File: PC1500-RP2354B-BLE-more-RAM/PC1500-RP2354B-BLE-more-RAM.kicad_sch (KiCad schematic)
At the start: 41 parts, among them J1 microSD, J2 USB-C (programming/debug), J3 PC-1500 40-pin cartridge slot, J5 PC1500_SENSE_JUMPER, J7 SWD_I2C_HEADER, SW1 BOOTSEL, U1 RP2354B, U10 TCA9406DCUR, U2 AS6C1008-55TINL, U3 SLG46826V, U4 AP2112K-3.3, U5 MCP6541T-I/LT, U8 BGM220SC22WGA2, U9 SLG46826V, X1 12MHz (Abracon ABM8-272-T3)

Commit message: More-RAM card: BLE_MODULE_WAKE (GPIO27 to BGM220S PB03); I2C pull-ups
- BLE_MODULE_WAKE: the MCU-to-module wake (an EM4 wake pin on the
  module), lost in the bus rewire. Pads updated; routing left for later.
- R25/R26: 1.5K pull-ups from SDA/SCL to +3V3.

Co-Authored-By: Claude Opus 5.5 <noreply@anthropic.com>
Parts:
- added R25, R26: 1.5K, Resistor_SMD:R_0201_0603Metric, symbol Device:R
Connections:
- net +3V3: now also R25.1, R26.1
- net SCL: now also R26.2
- net SCL_GP: no longer J7.1 (Pin_1)
- net SDA: now also R25.2
- net SDA_GP: no longer J7.3 (Pin_3)
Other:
- moved on the sheet: J7

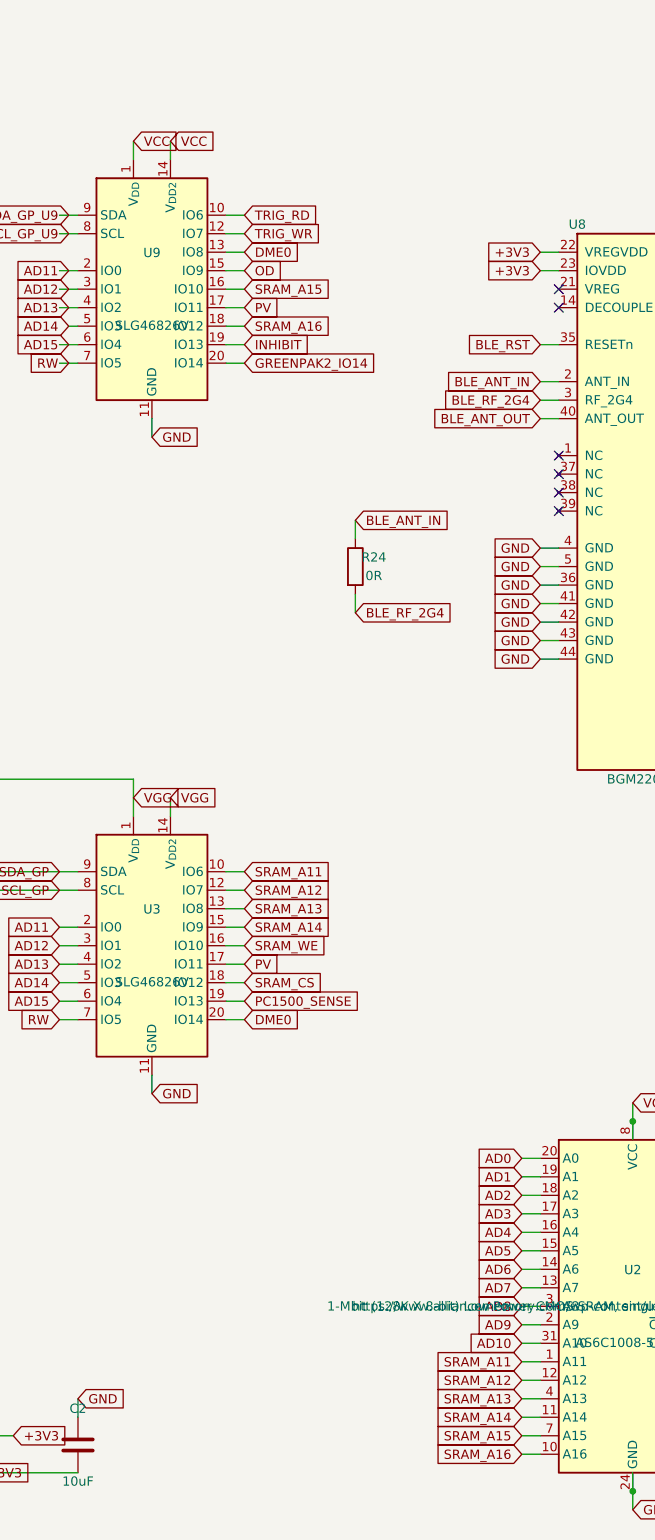
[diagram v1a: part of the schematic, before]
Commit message: More-RAM card schematic: SRAM A11-A13 from the bus, GP1 drives A14-A16, INHIBIT on GP1, GP2 on VGG
- SRAM A11-A13 come straight from AD11-AD13; GP1 (U3) IO7/IO8/IO9 drive
  SRAM_A14/15/16 (the card GP1 design).
- INHIBIT (J3 pin 15) moved to GP1 IO6 (U3 pin 10); GP2 IO10/IO12/IO13 are
  no-connects.
- GP2 (U9) VDD/VDD2 moved from VCC to VGG, as on the dongle: both GreenPAKs
  keep their state through power-off.
Schematic only; the PCB still has the old nets and needs re-routing.

Co-Authored-By: Claude Opus 5.5 <noreply@anthropic.com>
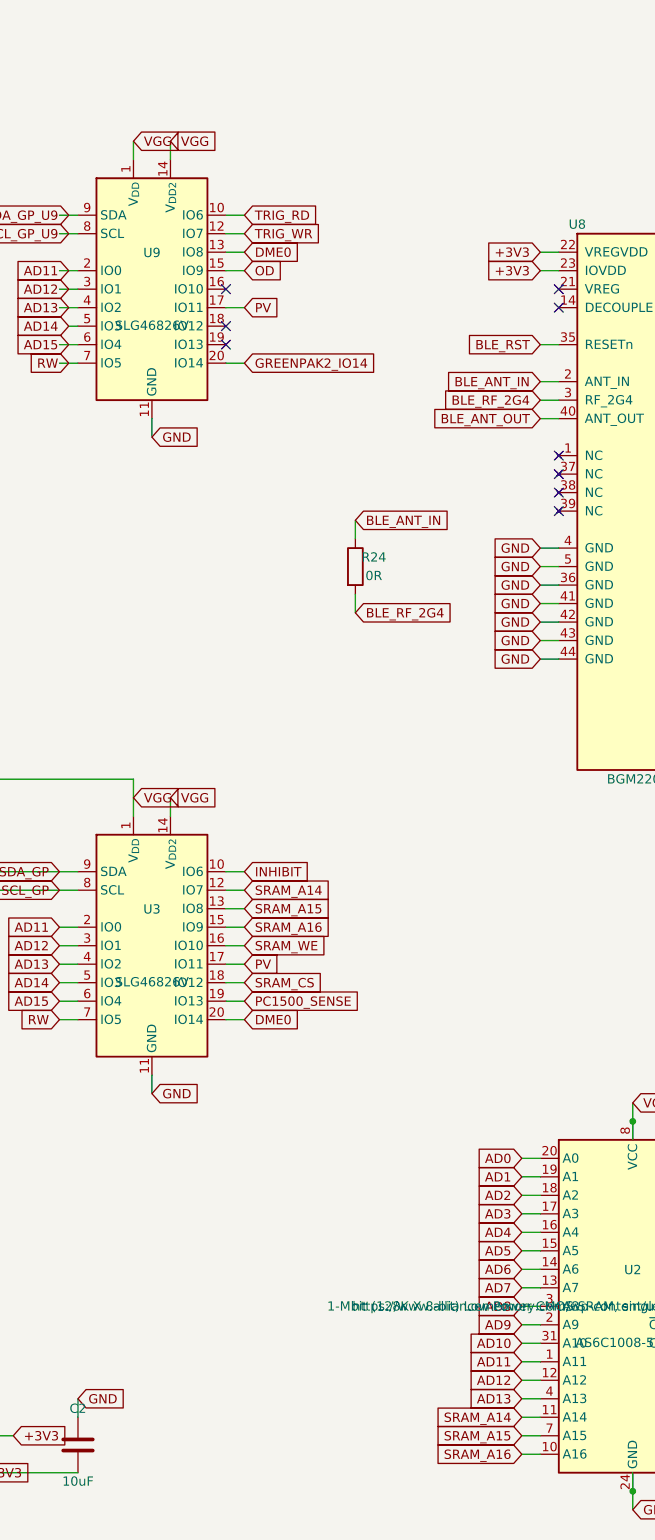
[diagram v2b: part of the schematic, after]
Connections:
- net AD11: now also U2.1 (A11)
- net AD12: now also U2.12 (A12)
- net AD13: now also U2.4 (A13)
- net INHIBIT: now also U3.10 (IO6); no longer U9.19 (IO13)
- net SRAM_A14: now also U3.12 (IO7); no longer U3.15 (IO9)
- net SRAM_A15: now also U3.13 (IO8); no longer U9.16 (IO10)
- net SRAM_A16: now also U3.15 (IO9); no longer U9.18 (IO12)
- net VCC: no longer U9.1 (V_{DD}), U9.14 (V_{DD2})
- net VGG: now also U9.1 (V_{DD}), U9.14 (V_{DD2})
- removed net SRAM_A11: U2.1 (A11), U3.10 (IO6)
- removed net SRAM_A12: U2.12 (A12), U3.12 (IO7)
- removed net SRAM_A13: U2.4 (A13), U3.13 (IO8)
- no-connect marks 29 -> 32
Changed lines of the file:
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@@
 		)
 	)
-	(wire
-		(pts
-			(xy 139.7 95.25) (xy 142.24 95.25)
-		)
-		(stroke
-			(width 0)
-			(type default)
-		)
+	(no_connect
+		(at 139.7 95.25)
 	)
 	(wire
@@
 		)
 	)
-	(wire
-		(pts
-			(xy 139.7 90.17) (xy 142.24 90.17)
-		)
-		(stroke
-			(width 0)
-			(type default)
-		)
+	(no_connect
+		(at 139.7 90.17)
 	)
 	(wire
@@
 		)
 	)
-	(wire
-		(pts
-			(xy 139.7 97.79) (xy 142.24 97.79)
-		)
-		(stroke
-			(width 0)
-			(type default)
-		)
+	(no_connect
+		(at 139.7 97.79)
 	)
 	(wire
@@
 		)
 	)
+	(global_label "INHIBIT"
+		(shape input)
+		(at 142.24 170.18 0)
+		(effects
+			(font
+				(size 1.27 1.27)
+			)
+			(justify left)
+		)
+		(property "Intersheetrefs" "${INTERSHEET_REFS}"
+			(at 142.24 170.18 0)
+			(hide yes)
+			(show_name no)
+			(do_not_autoplace no)
+			(effects
+				(font
+					(size 1.27 1.27)
+				)
+			)
+		)
+	)
 	(wire
 		(pts
@@
 		)
 	)
-	(global_label "VCC"
+	(global_label "VGG"
 		(shape input)
 		(at 132.08 69.85 0)
@@
 		)
 	)
-	(global_label "SRAM_A12"
+	(global_label "AD12"
 		(shape input)
 		(at 180.34 240.03 180)
@@
 		)
 	)
-	(global_label "SRAM_A15"
-		(shape input)
-		(at 142.24 90.17 0)
-		(effects
-			(font
-				(size 1.27 1.27)
-			)
-			(justify left)
-		)
-		(property "Intersheetrefs" "${INTERSHEET_REFS}"
-			(at 142.24 90.17 0)
-			(hide yes)
-			(show_name no)
-			(do_not_autoplace no)
-			(effects
-				(font
-					(size 1.27 1.27)
-				)
-			)
-		)
-	)
 	(global_label "AD8"
 		(shape input)
@@
 		)
 	)
-	(global_label "SRAM_A13"
+	(global_label "AD13"
 		(shape input)
 		(at 180.34 242.57 180)
@@
 		)
 	)
-	(global_label "SRAM_A12"
+	(global_label "SRAM_A14"
 		(shape input)
 		(at 142.24 172.72 0)
@@
 		)
 	)
-	(global_label "INHIBIT"
-		(shape input)
-		(at 142.24 97.79 0)
-		(effects
-			(font
-				(size 1.27 1.27)
-			)
-			(justify left)
-		)
-		(property "Intersheetrefs" "${INTERSHEET_REFS}"
-			(at 142.24 97.79 0)
-			(hide yes)
-			(show_name no)
-			(do_not_autoplace no)
-			(effects
-				(font
-					(size 1.27 1.27)
-				)
-			)
-		)
-	)
 	(global_label "TRIG_WR"
 		(shape input)
@@
 		)
 	)
-	(global_label "SRAM_A14"
+	(global_label "SRAM_A16"
 		(shape input)
 		(at 142.24 177.8 0)
@@
 		)
 	)
-	(global_label "SRAM_A11"
-		(shape input)
-		(at 142.24 170.18 0)
-		(effects
-			(font
-				(size 1.27 1.27)
-			)
-			(justify left)
-		)
-		(property "Intersheetrefs" "${INTERSHEET_REFS}"
-			(at 142.24 170.18 0)
-			(hide yes)
-			(show_name no)
-			(do_not_autoplace no)
-			(effects
-				(font
-					(size 1.27 1.27)
-				)
-			)
-		)
-	)
 	(global_label "SD_CS"
 		(shape input)
@@
 		)
 	)
-	(global_label "SRAM_A13"
+	(global_label "SRAM_A15"
 		(shape input)
 		(at 142.24 175.26 0)
@@
 		)
 	)
-	(global_label "SRAM_A11"
+	(global_label "AD11"
 		(shape input)
 		(at 180.34 237.49 180)
@@
 		)
 	)
-	(global_label "VCC"
+	(global_label "VGG"
 		(shape input)
 		(at 127 69.85 0)
@@
 			(hide yes)
 			(show_name no)
-			(do_not_autoplace no)
-			(effects
-				(font
-					(size 1.27 1.27)
-				)
-			)
-		)
-	)
-	(global_label "SRAM_A16"
-		(shape input)
-		(at 142.24 95.25 0)
-		(effects
-			(font
-				(size 1.27 1.27)
-			)
-			(justify left)
-		)
-		(property "Intersheetrefs" "${INTERSHEET_REFS}"
-			(at 142.24 95.25 0)
-			(hide yes)
-			(show_name no)

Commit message: More-RAM card: GP2 INHIBIT/MCU_READY/TRIG_WR_SYS, test points, USB 27R, decoupling, Abracon L2; placed and routed
Schematic:
- INHIBIT from GP2 (U9) IO10; U9 IO14 = MCU_READY -> GPIO25; U9 IO12 =
  TRIG_WR_SYS (7000-7FFF write trigger) -> GPIO24.
- Test points: TP4 on GPIO46; TP9 GP1_IO6, TP10 GP2_IO13, TP11 card-edge PU.
- USB-C D+/D- pairing fixed; R27/R28 27R series resistors.
- Decoupling per Raspberry Pi's "Hardware design with RP2350": 100nF per
  RP2354B power pin, 4.7uF on VREG_VIN and DVDD, R29 33R + C27 4.7uF on
  VREG_AVDD (FLG5). One 100nF per GreenPAK at VDD, two on the SRAM.
- L2 = Abracon AOTA-B201610S3R3-101-T (LCSC C42411119) on a new
  Sharp-PC-Footprints:L_Abracon_AOTA-B201610 footprint, generated by
  tools/gen_fp_abracon_aota_b201610.py from Abracon's land pattern.
- TP values follow their nets.

PCB: new parts placed and routed; DVDD 4.7uF moved next to L2's output;
XOUT straightened; reference designators restored to match the schematic
(silkscreen labels kept as Value fields / ${REFERENCE} texts). DRC: 0
unconnected, schematic parity only the PWR_FLAGs; remaining clearance
errors are the J1 shell vias (expected, see DESIGN_DECISIONS.md).
Design rules updated in the .kicad_pro.

Co-Authored-By: Claude Opus 5.5 <noreply@anthropic.com>
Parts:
- added C15, C16, C17, C18, C19, C20, C21, C23, C24, C25, C29, C30, C31, C32: 100nF, Capacitor_SMD:C_0402_1005Metric, symbol Device:C
- added C22, C26, C27: 4.7uF, Capacitor_SMD:C_0402_1005Metric, symbol Device:C
- added R27, R28: 27R, Resistor_SMD:R_0402_1005Metric, symbol Device:R
- added R29: 33R, Resistor_SMD:R_0402_1005Metric, symbol Device:R
- added TP10: GP2_IO13, TestPoint:TestPoint_Pad_1.0x1.0mm, symbol Connector:TestPoint
- added TP11: PU, TestPoint:TestPoint_Pad_1.0x1.0mm, symbol Connector:TestPoint
- added TP9: GP1_IO6, TestPoint:TestPoint_Pad_1.0x1.0mm, symbol Connector:TestPoint
- L2: value 1uH -> 3.3uH (Abracon AOTA-B201610S3R3-101-T); footprint Inductor_SMD:L_0805_2012Metric -> Sharp-PC-Footprints:L_Abracon_AOTA-B201610; LCSC (none) -> C42411119
- TP4: value GPIO19 -> GPIO46
- TP5: value GPIO20 -> GPIO26
- TP8: value GPIO34 -> GPIO47
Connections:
- net +3V3: now also C15.1, C16.1, C17.1, C18.1, C19.1, C20.1, C21.1, C22.1, R29.1; no longer U1.61 (VREG_AVDD)
- net DVDD: now also C23.1, C24.1, C25.1, C26.1
- net GND: now also C15.2, C16.2, C17.2, C18.2, C19.2, C20.2, C21.2, C22.2, C23.2, C24.2, C25.2, C26.2, C27.2, C29.2, C30.2, C31.2, C32.2
- net GPIO46: now also TP4.1
- net INHIBIT: now also U9.16 (IO10); no longer U3.10 (IO6)
- net PU: now also TP11.1
- net SCL_GP: now also J7.1 (Pin_1)
- net SDA_GP: now also J7.3 (Pin_3)
- net USB_DM: now also R28.2; no longer J2.A6 (D+), J2.B7 (D-)
- net USB_DP: now also R27.2; no longer J2.A7 (D-), J2.B6 (D+)
- net VGG: now also C29.1, C30.1, C31.1, C32.1
- net TRIG_WR_SYS: now reaches U9.18 (IO12)
- net TRIG_WR_SYS: now also U1.25 (GPIO24)
- net GP2_IO13: now reaches U9.19 (IO13)
- net GP2_IO13: now also TP10.1
- removed net GPIO24: TP4.1, U1.25 (GPIO24)
- net GREENPAK2_IO14 renamed MCU_READY
- new net GP1_IO6: TP9.1, U3.10 (IO6)
- new net USB_C_DM: J2.A7 (D-), J2.B7 (D-), R28.1
- new net USB_C_DP: J2.A6 (D+), J2.B6 (D+), R27.1
- new net VREG_AVDD: C27.1, R29.2, U1.61 (VREG_AVDD)
- no-connect marks 32 -> 29
